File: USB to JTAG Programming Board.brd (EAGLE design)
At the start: 45.1 x 48.3 mm, 48 parts, among them CON1 UBC05V128-B0C04D, Q3 12M, U17 TPS62162DSGR, U5 ISO7240, U6 FT2232H, U7 ISO7231, U8 93LC56BT-I/OT

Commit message: Created Gerbs, updated parts to order
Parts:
- moved U$2 37.4 mm to (43.2, 30.0), flipped to the bottom
- moved LOGO1 29.3 mm to (16.8, 49.3), flipped to the bottom
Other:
- board size 45.1 x 48.3 mm -> 45.1 x 34 mm
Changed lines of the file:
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@@
 <board>
 <plain>
-<wire x1="0.008746875" y1="57.7108625" x2="0.008746875" y2="18.00196875" width="0" layer="20"/>
-<wire x1="0.008746875" y1="18.00196875" x2="4.294715625" y2="13.716" width="0" layer="20" curve="90"/>
-<wire x1="4.294715625" y1="13.716" x2="40.500190625" y2="13.716" width="0" layer="20"/>
-<wire x1="40.500190625" y1="13.716" x2="45.136" y2="18.351809375" width="0" layer="20" curve="90"/>
-<wire x1="45.136" y1="18.351809375" x2="45.136" y2="57.94504375" width="0" layer="20"/>
+<wire x1="0.008746875" y1="57.7108625" x2="0.008746875" y2="31.736884375" width="0" layer="20"/>
+<wire x1="0.008746875" y1="31.736884375" x2="3.80563125" y2="27.94" width="0" layer="20" curve="90"/>
+<wire x1="3.80563125" y1="27.94" x2="40.510315625" y2="27.94" width="0" layer="20"/>
+<wire x1="40.510315625" y1="27.94" x2="45.136" y2="32.565684375" width="0" layer="20" curve="90"/>
+<wire x1="45.136" y1="32.565684375" x2="45.136" y2="57.94504375" width="0" layer="20"/>
 <wire x1="45.136" y1="57.94504375" x2="41.115109375" y2="61.9881625" width="0" layer="20" curve="89.662897"/>
 <wire x1="41.115109375" y1="61.9881625" x2="4.277715625" y2="61.9881625" width="0" layer="20"/>
 <wire x1="4.277715625" y1="61.9881625" x2="0.008746875" y2="57.7108625" width="0" layer="20" curve="90.284396"/>
-<text x="1.27" y="21.59" size="1.27" layer="21" font="vector">USB to JTAG IC Programming Board
+<text x="42.672" y="52.578" size="1.27" layer="22" font="vector" rot="MR0">USB to JTAG IC Programming Board
 Mars Rover 2017 Rev 1
 Missouri S&amp;T
@@
 </element>
 <element name="U$1" library="MRDT-Connectors" package="1.27MM_2X5_BOX_HEADER_STRAIGHT" value="1175-1733-ND" x="42.926" y="53.086" smashed="yes" rot="R180"/>
-<element name="U$2" library="MRDT-Signatures" package="ANDREW_VAN_HORN_SIGNATURE" value="ANDREW_VAN_HORN_SIGNATURE" x="9.144" y="14.478"/>
-<element name="LOGO1" library="MRDT-Hardware" package="MRDT_LOGO" value="MRDT_LOGO" x="33.02" y="24.892"/>
+<element name="U$2" library="MRDT-Signatures" package="ANDREW_VAN_HORN_SIGNATURE" value="ANDREW_VAN_HORN_SIGNATURE" x="43.18" y="29.972" rot="MR0"/>
+<element name="LOGO1" library="MRDT-Hardware" package="MRDT_LOGO" value="MRDT_LOGO" x="16.764" y="49.276" rot="MR0"/>
 </elements>
 <signals>
@@
 <vertex x="1.016" y="61.468"/>
 <vertex x="44.45" y="61.468"/>
-<vertex x="44.45" y="26.924"/>
-<vertex x="0.254" y="26.924"/>
+<vertex x="44.704" y="28.448"/>
+<vertex x="0.254" y="28.448"/>
 <vertex x="0.254" y="60.452"/>
 </polygon>
@@
 <vertex x="0.762" y="61.214"/>
 <vertex x="44.704" y="61.214"/>
-<vertex x="44.704" y="28.702"/>
-<vertex x="44.958" y="26.924"/>
-<vertex x="0.508" y="26.924"/>
+<vertex x="44.704" y="28.448"/>
+<vertex x="0.254" y="28.448"/>
 <vertex x="0.508" y="60.706"/>
 <vertex x="0.762" y="60.96"/>

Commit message: Updated Gerber Files; Final changes to board design
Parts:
- moved U$2 1.02 mm to (44.2, 30.0)
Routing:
- net AGND: track 22.3 -> 24.1 mm, vias 9 -> 14
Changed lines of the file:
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@@
 <layer number="13" name="Route13" color="4" fill="5" visible="no" active="yes"/>
 <layer number="14" name="Route14" color="1" fill="6" visible="no" active="yes"/>
-<layer number="15" name="Route15" color="4" fill="6" visible="yes" active="yes"/>
+<layer number="15" name="Route15" color="4" fill="6" visible="no" active="yes"/>
 <layer number="16" name="Bottom" color="1" fill="1" visible="yes" active="yes"/>
 <layer number="17" name="Pads" color="2" fill="1" visible="yes" active="yes"/>
@@
 <wire x1="41.115109375" y1="61.9881625" x2="4.277715625" y2="61.9881625" width="0" layer="20"/>
 <wire x1="4.277715625" y1="61.9881625" x2="0.008746875" y2="57.7108625" width="0" layer="20" curve="90.284396"/>
-<text x="42.672" y="52.578" size="1.27" layer="22" font="vector" rot="MR0">USB to JTAG IC Programming Board
+<text x="12.954" y="59.69" size="1.27" layer="22" font="vector" rot="MR180">USB to JTAG IC Programming Board
 Mars Rover 2017 Rev 1
 Missouri S&amp;T
@@
 </element>
 <element name="C17" library="rcl" package="C0402" value="36p" x="14.478" y="43.18" smashed="yes" rot="MR270">
-<attribute name="NAME" x="14.859" y="41.529" size="0.8128" layer="26" font="vector" rot="MR270"/>
+<attribute name="NAME" x="14.859" y="46.609" size="0.8128" layer="26" font="vector" rot="MR270"/>
 <attribute name="VALUE" x="16.383" y="43.815" size="1.27" layer="28" rot="MR270"/>
 </element>
 <element name="C18" library="rcl" package="C0402" value="36p" x="15.748" y="44.958" smashed="yes" rot="MR90">
-<attribute name="NAME" x="15.367" y="41.529" size="0.8128" layer="26" font="vector" rot="MR90"/>
+<attribute name="NAME" x="15.367" y="46.609" size="0.8128" layer="26" font="vector" rot="MR90"/>
 <attribute name="VALUE" x="13.843" y="44.323" size="1.27" layer="28" rot="MR90"/>
 </element>
@@
 </element>
 <element name="F1" library="rcl" package="L1812" value="500mA" x="12.7" y="37.846" smashed="yes" rot="MR90">
-<attribute name="NAME" x="14.605" y="35.941" size="0.8128" layer="26" font="vector" rot="MR90"/>
+<attribute name="NAME" x="14.351" y="37.465" size="1.27" layer="26" rot="MR90"/>
 <attribute name="VALUE" x="9.525" y="35.941" size="1.27" layer="28" rot="MR90"/>
 </element>
@@
 <attribute name="MF" value="" x="19.558" y="43.688" size="1.778" layer="28" rot="MR90" display="off"/>
 <attribute name="MPN" value="" x="19.558" y="43.688" size="1.778" layer="28" rot="MR90" display="off"/>
-<attribute name="NAME" x="20.828" y="42.037" size="0.8128" layer="26" font="vector" ratio="10" rot="MR90"/>
+<attribute name="NAME" x="22.606" y="40.259" size="0.8128" layer="26" font="vector" ratio="10" rot="MR90"/>
 <attribute name="OC_FARNELL" value="unknown" x="19.558" y="43.688" size="1.778" layer="28" rot="MR90" display="off"/>
 <attribute name="OC_NEWARK" value="unknown" x="19.558" y="43.688" size="1.778" layer="28" rot="MR90" display="off"/>
@@
 </element>
 <element name="U$1" library="MRDT-Connectors" package="1.27MM_2X5_BOX_HEADER_STRAIGHT" value="1175-1733-ND" x="42.926" y="53.086" smashed="yes" rot="R180"/>
-<element name="U$2" library="MRDT-Signatures" package="ANDREW_VAN_HORN_SIGNATURE" value="ANDREW_VAN_HORN_SIGNATURE" x="43.18" y="29.972" rot="MR0"/>
+<element name="U$2" library="MRDT-Signatures" package="ANDREW_VAN_HORN_SIGNATURE" value="ANDREW_VAN_HORN_SIGNATURE" x="44.196" y="29.972" rot="MR0"/>
 <element name="LOGO1" library="MRDT-Hardware" package="MRDT_LOGO" value="MRDT_LOGO" x="16.764" y="49.276" rot="MR0"/>
 </elements>
@@
 <wire x1="11.608" y1="34.544" x2="9.144" y2="34.544" width="0.254" layer="1"/>
 <via x="9.144" y="34.544" extent="1-16" drill="0.35"/>
+<via x="17.78" y="46.236" extent="1-16" drill="0.35"/>
+<wire x1="11.998" y1="48.6114" x2="11.3926" y2="48.006" width="0.1524" layer="1"/>
+<wire x1="11.3926" y1="48.006" x2="10.414" y2="48.006" width="0.1524" layer="1"/>
+<via x="10.414" y="48.006" extent="1-16" drill="0.35"/>
+<via x="20.828" y="43.942" extent="1-16" drill="0.35"/>
+<via x="3.048" y="58.928" extent="1-16" drill="0.35"/>
+<via x="10.16" y="38.608" extent="1-16" drill="0.35"/>
 </signal>
 <signal name="FTDI_3V3">

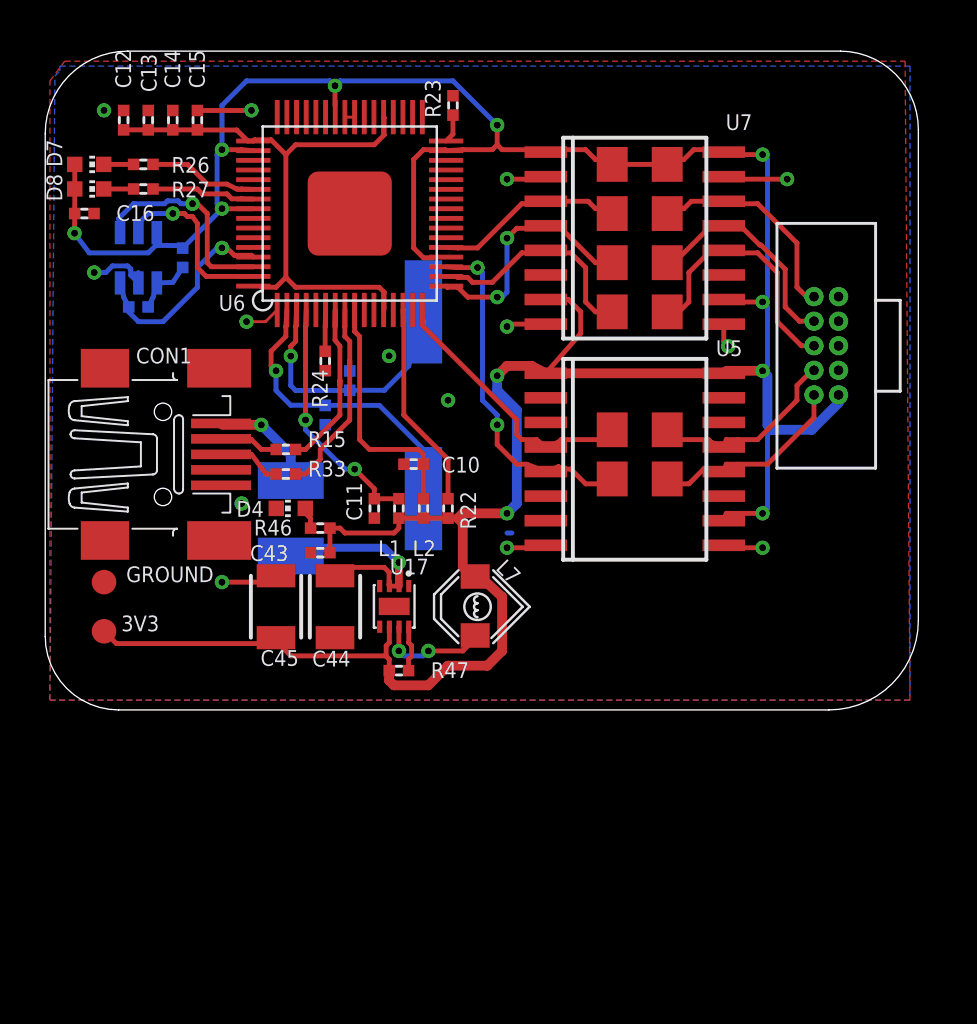
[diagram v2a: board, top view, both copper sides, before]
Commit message: Changed footprint of FTDI chip
The solder pads were too close to the chip, and as such most of the pad was underneath the chip. The pads were moved and the circuit modified.
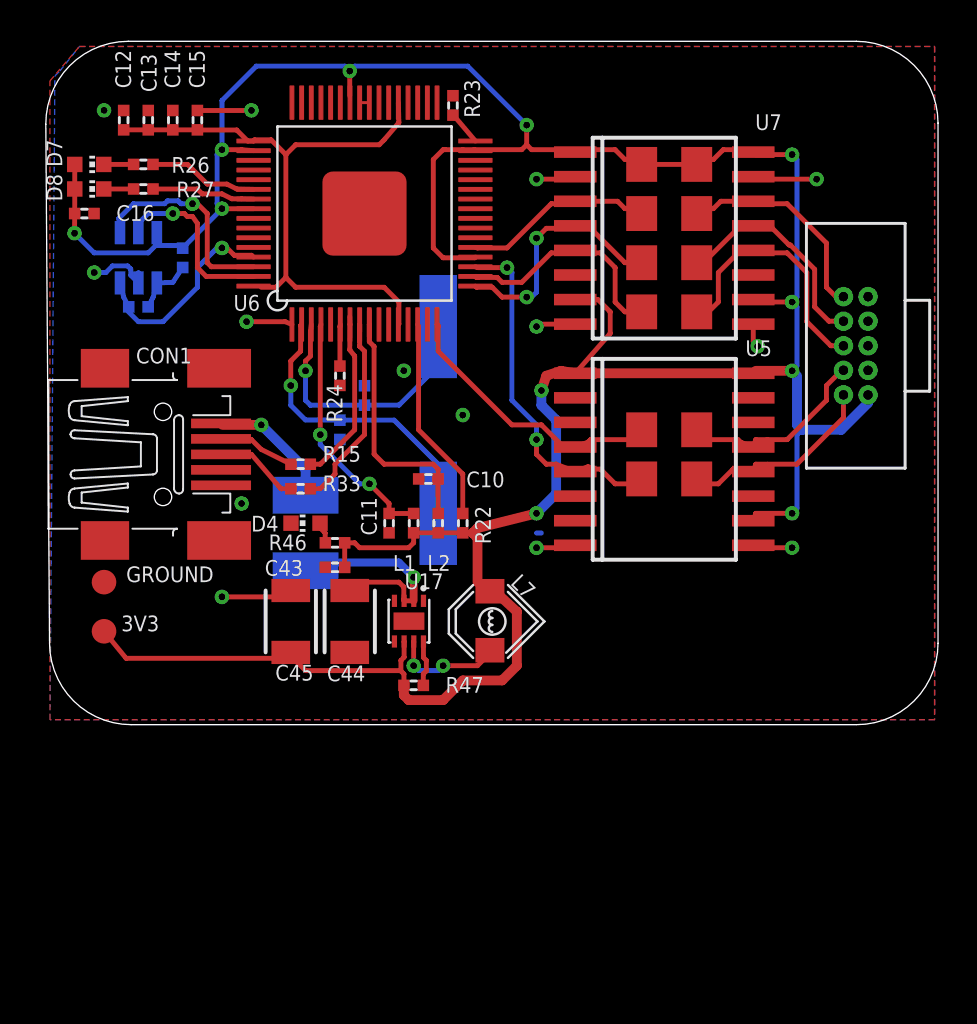
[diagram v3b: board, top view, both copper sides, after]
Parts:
- moved LOGO1 6.61 mm to (23.4, 49.0)
- moved U$2 2.84 mm to (46.7, 28.7)
- moved R18 1.52 mm to (32.3, 39.9)
- moved R19 1.52 mm to (32.3, 51.1)
- moved R20 1.52 mm to (32.3, 42.4)
- moved R21 1.52 mm to (32.3, 56.1)
- moved R28 1.52 mm to (32.3, 53.6)
- moved R32 1.52 mm to (32.3, 48.5)
- moved U$1 1.52 mm to (44.5, 53.1)
- moved U5 1.52 mm to (32.0, 40.9)
- moved U7 1.52 mm to (32.0, 52.3)
- moved C18 1.08 mm to (16.5, 44.2)
- moved C10 1.08 mm to (19.8, 39.9)
- moved C11 1.08 mm to (17.8, 37.6)
- moved C17 1.08 mm to (15.2, 42.4)
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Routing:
- net FTDI_3V3: track 167.2 -> 171.4 mm
- net FTDI_1V8: track 30.0 -> 32.4 mm
- net AGND: track 24.1 -> 25.4 mm
- net XUSB: track 5.62 -> 6.70 mm
- net N$39: track 3.36 -> 4.43 mm
- net N$38: track 3.06 -> 4.00 mm
- net N$26: track 13.2 -> 14.1 mm
- net D-: track 9.66 -> 8.96 mm
- net D+: track 10.3 -> 10.9 mm
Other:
- board size 45.1 x 34 mm -> 46.1 x 35.3 mm
